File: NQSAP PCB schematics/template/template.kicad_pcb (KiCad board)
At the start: 2 copper layers, 102 x 96 mm, 6 parts, among them J1 Bus, J2 Bus, J3 Conn_02x08, J4 Conn_02x08, J5 Conn_02x08, J6 Conn_02x08

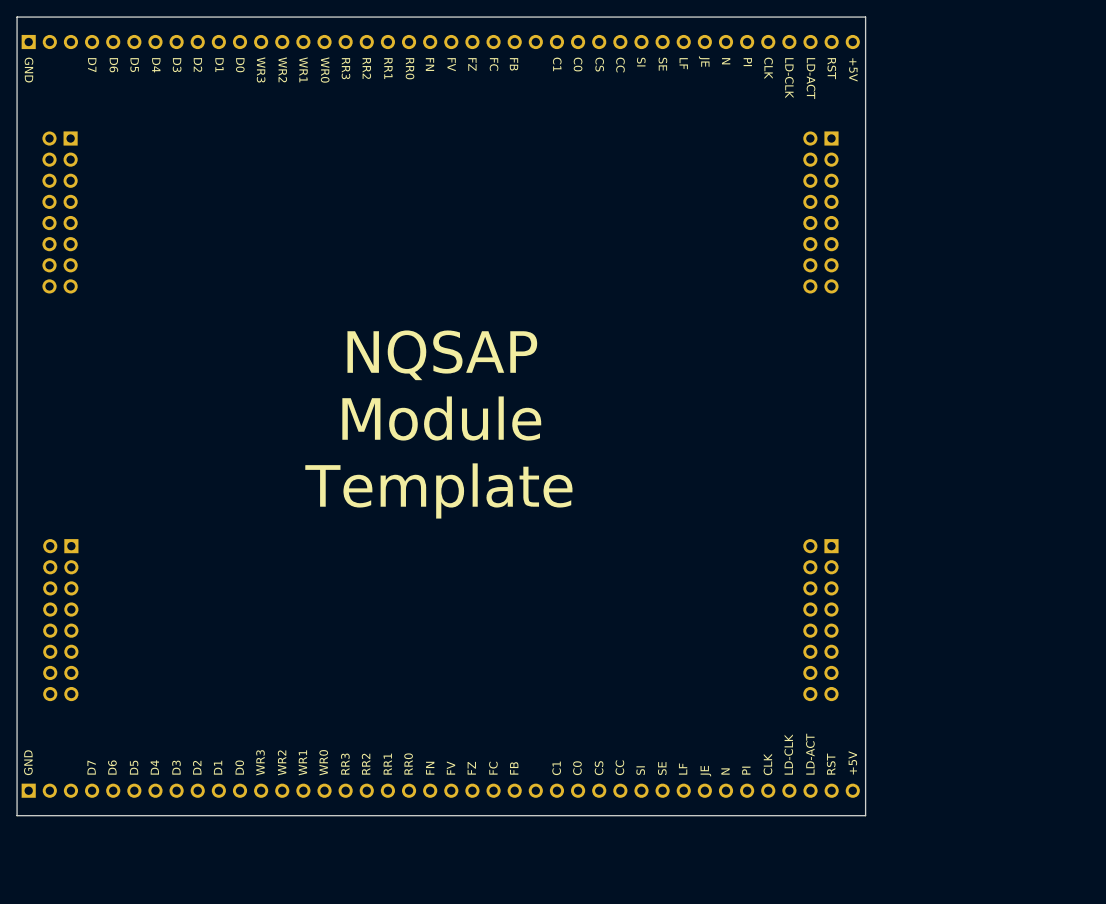
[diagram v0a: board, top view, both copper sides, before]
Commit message: Add RAM, update and add gerbers for new boards
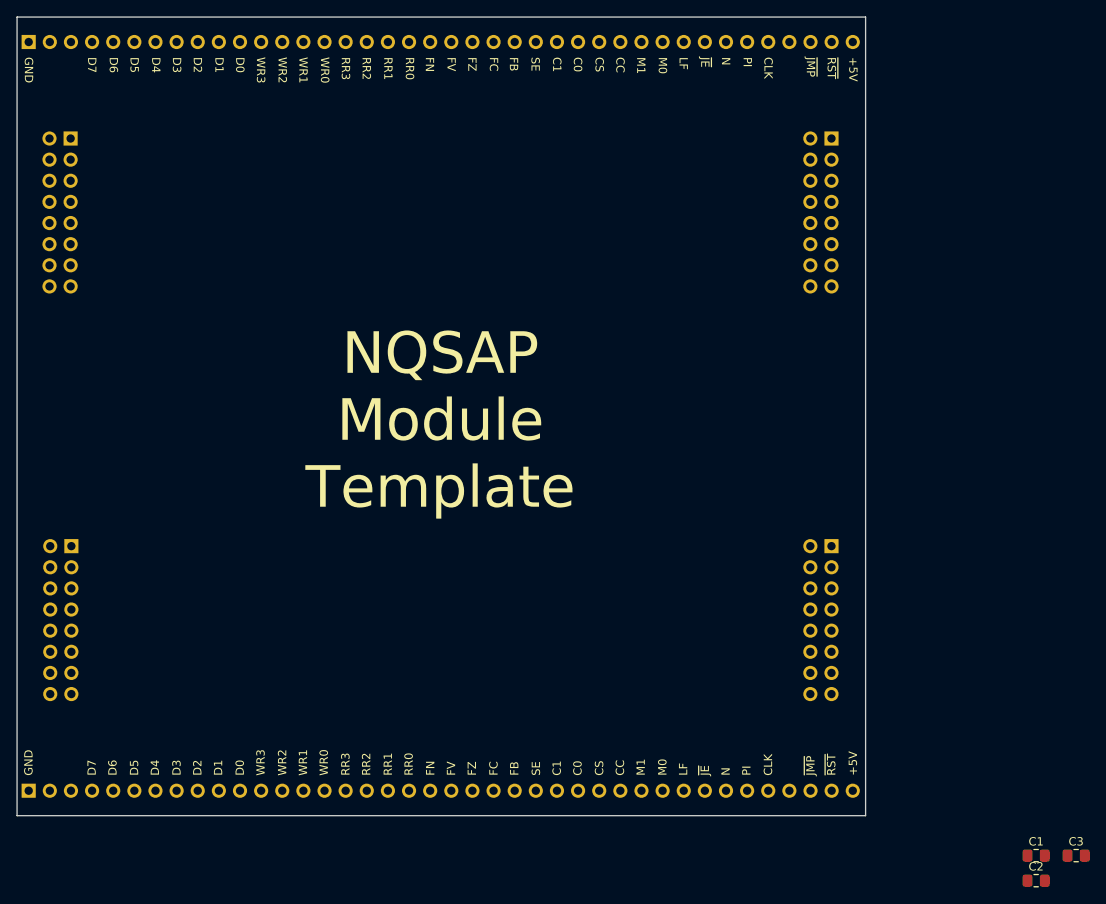
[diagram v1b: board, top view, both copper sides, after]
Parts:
- added C1: 0.1uF, Capacitor_SMD:C_0805_2012Metric_Pad1.18x1.45mm_HandSolder, F.Cu at (207.5, 143.8)
- added C2: 0.1uF, Capacitor_SMD:C_0805_2012Metric_Pad1.18x1.45mm_HandSolder, F.Cu at (207.5, 146.8)
- added C3: 0.1uF, Capacitor_SMD:C_0805_2012Metric_Pad1.18x1.45mm_HandSolder, F.Cu at (212.3, 143.8)
- J3: value Conn_02x08 -> IC-TL
- J4: value Conn_02x08 -> IC-BL
- J5: value Conn_02x08 -> IC-TR
- J6: value Conn_02x08 -> IC-BR
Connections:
- net LDR-ACT renamed ~JMP
- net RST renamed ~RST
- net SI renamed M1
- J1 pad 2: NC-2 -> Net-(J1-Pad2)
- J1 pad 25: XX0 -> SE
- J1 pad 3: NC-1 -> Net-(J1-Pad3)
- J1 pad 31: SE -> M0
- J1 pad 37: LDR-CLK -> Net-(J1-Pad37)
- J2 pad 2: NC-2 -> Net-(J2-Pad2)
- J2 pad 25: XX0 -> SE
- J2 pad 3: NC-1 -> Net-(J2-Pad3)
- J2 pad 31: SE -> M0
- J2 pad 37: LDR-CLK -> Net-(J2-Pad37)
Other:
- board text added: "M0"
- board text added: "M1"
- board text added: "~JE"
- board text added: "~JMP"
- board text added: "~RST"
- board text removed: "JE"
- board text removed: "LD-ACT"
- board text removed: "LD-CLK"
- board text removed: "RST"
- board text removed: "SI"
